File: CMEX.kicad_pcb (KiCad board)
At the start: 2 copper layers, 4 parts, among them U1 DAC63004RTET, U2 TPS62151, U3 ADS8584S

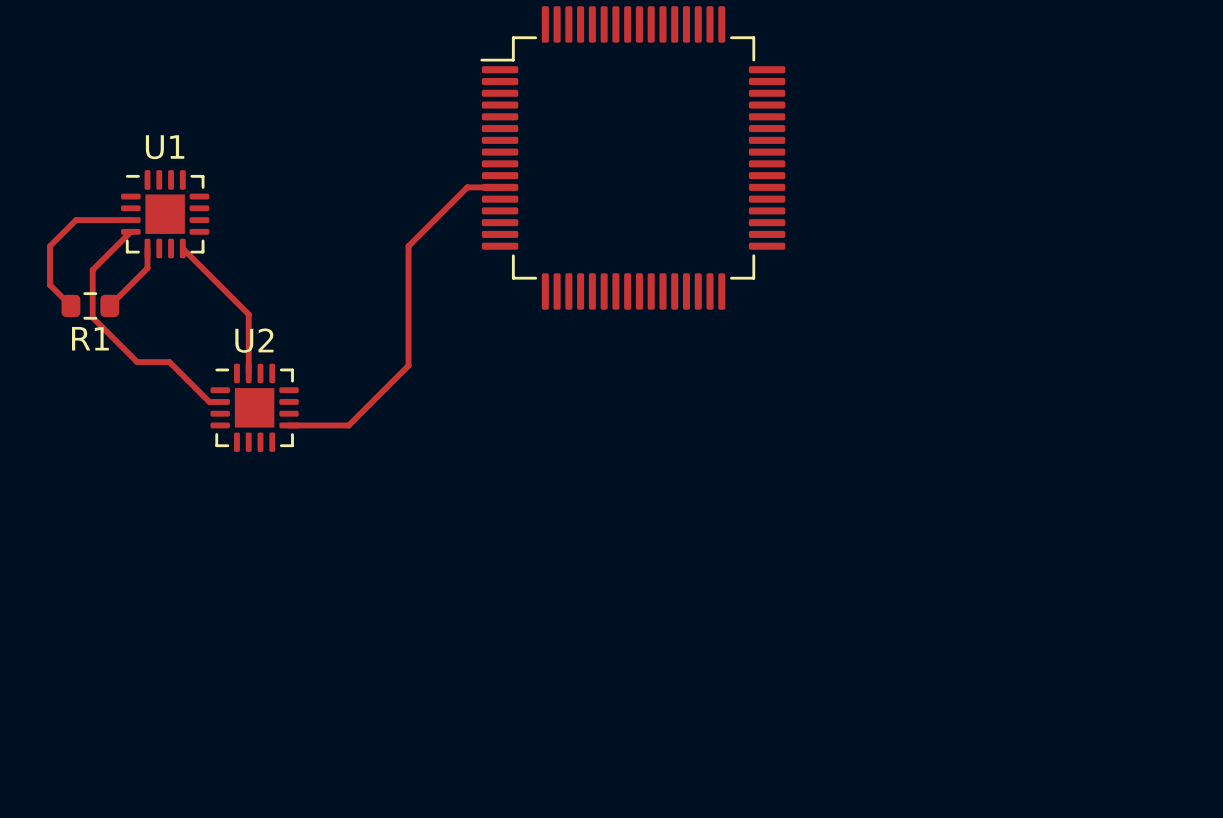
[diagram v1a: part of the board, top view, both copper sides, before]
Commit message: Added connector to all sheets.
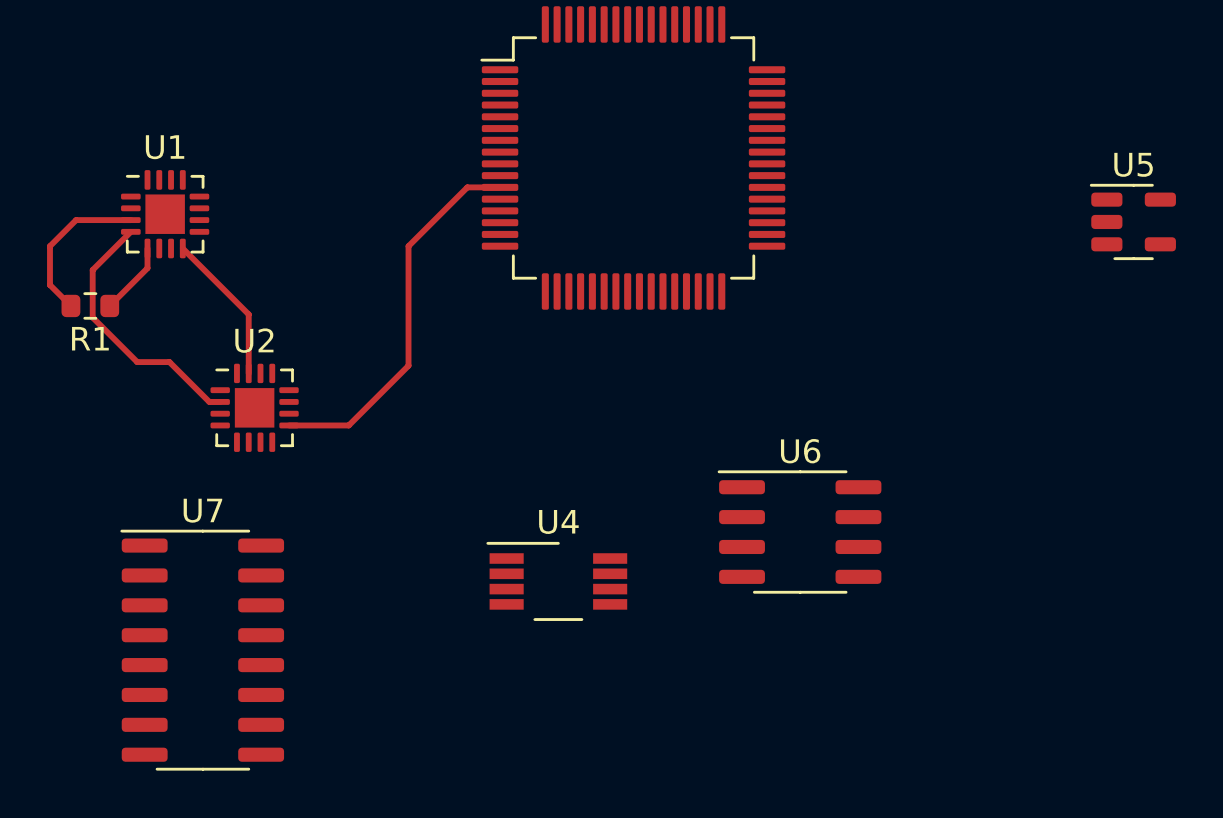
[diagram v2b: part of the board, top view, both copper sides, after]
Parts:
- added U4: TLV8802, Package_SO:VSSOP-8_3.0x3.0mm_P0.65mm, F.Cu at (67.3, 44.7)
- added U5: TLV8801, Package_TO_SOT_SMD:SOT-23-5, F.Cu at (91.8, 29.4)
- added U6: LMC7660, Package_SO:SOIC-8_3.9x4.9mm_P1.27mm, F.Cu at (77.6, 42.6)
- added U7: SN65MLVD047AD, Package_SO:SOIC-16_3.9x9.9mm_P1.27mm, F.Cu at (52.2, 47.6)

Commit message: Layout erster Entwurf fertig.
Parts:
- removed U4: TLV8802, Package_SO:VSSOP-8_3.0x3.0mm_P0.65mm
- added C1: C0402_100nF_50V, Capacitor_SMD:C_0402_1005Metric, F.Cu at (183.4, 132.6)
- added C10: C0402_22uF_6.3V, Capacitor_SMD:C_0402_1005Metric, F.Cu at (173.2, 139.8)
- added C11: C0402_1uF_6.3V, Capacitor_SMD:C_0402_1005Metric, F.Cu at (192.6, 139.1)
- added C12: C0402_100nF_50V, Capacitor_SMD:C_0402_1005Metric, F.Cu at (192.6, 138.1)
- added C15: C0402_330p_25V, Capacitor_SMD:C_0402_1005Metric, F.Cu at (182.0, 141.9)
- added C17: C0402_10uF_6.3V, Capacitor_SMD:C_0402_1005Metric, F.Cu at (182.0, 139.8)
- added C19: C0402_22uF_6.3V, Capacitor_SMD:C_0402_1005Metric, F.Cu at (183.3, 139.9)
- added C2: C0402_4.7uF_6.3V, Capacitor_SMD:C_0402_1005Metric, F.Cu at (184.7, 132.6)
- added C21: C0402_1uF_6.3V, Capacitor_SMD:C_0402_1005Metric, F.Cu at (196.0, 138.7)
- added C22: C0402_1uF_6.3V, Capacitor_SMD:C_0402_1005Metric, F.Cu at (197.8, 153.0)
- added C23: C0402_100nF_50V, Capacitor_SMD:C_0402_1005Metric, F.Cu at (197.8, 139.4)
- added C24: C0402_100nF_50V, Capacitor_SMD:C_0402_1005Metric, F.Cu at (197.3, 154.7)
- added C25: C0402_1uF_6.3V, Capacitor_SMD:C_0402_1005Metric, F.Cu at (189.2, 155.1)
- added C26: C0402_1uF_6.3V, Capacitor_SMD:C_0402_1005Metric, F.Cu at (183.8, 147.0)
- added C27: C0402_100nF_50V, Capacitor_SMD:C_0402_1005Metric, F.Cu at (190.3, 155.1)
- added C28: C0402_100nF_50V, Capacitor_SMD:C_0402_1005Metric, F.Cu at (183.8, 145.8)
- added C3: C0402_100nF_50V, Capacitor_SMD:C_0402_1005Metric, F.Cu at (183.3, 135.3)
- added C31: C0402_10uF_6.3V, Capacitor_SMD:C_0402_1005Metric, F.Cu at (194.2, 155.1)
- added C32: C0402_10uF_6.3V, Capacitor_SMD:C_0402_1005Metric, F.Cu at (193.0, 155.1)
- added C33: C0402_1uF_6.3V, Capacitor_SMD:C_0402_1005Metric, F.Cu at (191.6, 155.1)
- added C34: C0402_1uF_6.3V, Capacitor_SMD:C_0402_1005Metric, F.Cu at (188.0, 155.1)
- added C35: C0402_10nF_16V, Capacitor_SMD:C_0402_1005Metric, F.Cu at (214.9, 144.3)
- added C37: C0402_1uF_6.3V, Capacitor_SMD:C_0402_1005Metric, F.Cu at (216.0, 144.3)
- added C39: C0402_100nF_50V, Capacitor_SMD:C_0402_1005Metric, F.Cu at (217.2, 144.3)
- added C4: C0402_4.7uF_6.3V, Capacitor_SMD:C_0402_1005Metric, F.Cu at (184.6, 135.3)
- added C41: C0402_10nF_16V, Capacitor_SMD:C_0402_1005Metric, F.Cu at (211.6, 151.3)
- added C42: C0402_10nF_16V, Capacitor_SMD:C_0402_1005Metric, F.Cu at (206.8, 153.0)
- added C43: C0402_1uF_6.3V, Capacitor_SMD:C_0402_1005Metric, F.Cu at (210.6, 151.3)
- added C44: C0402_1uF_6.3V, Capacitor_SMD:C_0402_1005Metric, F.Cu at (206.8, 152.0)
- added C45: C0402_100nF_50V, Capacitor_SMD:C_0402_1005Metric, F.Cu at (212.7, 151.3)
- added C46: C0402_100nF_50V, Capacitor_SMD:C_0402_1005Metric, F.Cu at (206.8, 150.9)
- added C47: C0402_10nF_16V, Capacitor_SMD:C_0402_1005Metric, F.Cu at (217.1, 146.5)
- added C49: C0402_1uF_6.3V, Capacitor_SMD:C_0402_1005Metric, F.Cu at (215.0, 146.5)
- added C5: C0402_560p_10V, Capacitor_SMD:C_0402_1005Metric, F.Cu at (190.4, 136.1)
- added C51: C0402_100nF_50V, Capacitor_SMD:C_0402_1005Metric, F.Cu at (216.1, 146.5)
- added C53: C0402_10nF_16V, Capacitor_SMD:C_0402_1005Metric, F.Cu at (217.1, 148.6)
- added C54: C0402_1uF_6.3V, Capacitor_SMD:C_0402_1005Metric, F.Cu at (214.9, 148.6)
- added C55: C0402_10nF_16V, Capacitor_SMD:C_0402_1005Metric, F.Cu at (206.9, 139.2)
- added C56: C0402_100nF_50V, Capacitor_SMD:C_0402_1005Metric, F.Cu at (216.0, 148.6)
- added C57: C0402_100nF_50V, Capacitor_SMD:C_0402_1005Metric, F.Cu at (208.4, 151.2)
- added C58: C0402_1uF_6.3V, Capacitor_SMD:C_0402_1005Metric, F.Cu at (206.9, 140.3)
- added C59: C0402_100nF_50V, Capacitor_SMD:C_0402_1005Metric, F.Cu at (209.4, 151.2)
- added C6: C0402_330p_25V, Capacitor_SMD:C_0402_1005Metric, F.Cu at (172.7, 143.8)
- added C60: C0402_100nF_50V, Capacitor_SMD:C_0402_1005Metric, F.Cu at (206.9, 141.4)
- added C61: C0402_1uF_6.3V, Capacitor_SMD:C_0402_1005Metric, F.Cu at (169.0, 154.2)
- added C62: C0402_100nF_50V, Capacitor_SMD:C_0402_1005Metric, F.Cu at (169.0, 153.2)
- added C63: C0402_1uF_6.3V, Capacitor_SMD:C_0402_1005Metric, F.Cu at (177.7, 156.8)
- added C64: C0402_100nF_50V, Capacitor_SMD:C_0402_1005Metric, F.Cu at (176.2, 158.3)
- added C66: C0402_100nF_50V, Capacitor_SMD:C_0402_1005Metric, F.Cu at (166.8, 148.1)
- added C67: C0402_100nF_50V, Capacitor_SMD:C_0402_1005Metric, F.Cu at (175.5, 148.4)
- added C7: C0402_10uF_6.3V, Capacitor_SMD:C_0402_1005Metric, F.Cu at (173.2, 141.8)
- added C8: C0402_100nF_50V, Capacitor_SMD:C_0402_1005Metric, F.Cu at (190.9, 131.2)
- added C9: C0402_4.7uF_6.3V, Capacitor_SMD:C_0402_1005Metric, F.Cu at (190.9, 132.3)
- added J1: Conn_01x30, Connector_PinHeader_1.27mm:PinHeader_1x30_P1.27mm_Vertical, F.Cu at (192.3, 128.1)
- added L1: 2.2uH, Inductor_SMD:L_Coilcraft_XAL60xx_6.36x6.56mm, F.Cu at (170.3, 134.5)
- added L2: 2.2uH, Inductor_SMD:L_Coilcraft_XAL60xx_6.36x6.56mm, F.Cu at (178.6, 134.7)
- added R13: R0402_100, Resistor_SMD:R_0402_1005Metric, F.Cu at (203.4, 144.0)
- added R14: R0402_33k, Resistor_SMD:R_0402_1005Metric, F.Cu at (165.6, 149.1)
- added R15: R0402_33k, Resistor_SMD:R_0402_1005Metric, F.Cu at (176.8, 149.5)
- added R16: R0402_10k, Resistor_SMD:R_0402_1005Metric, F.Cu at (166.8, 150.2)
- added R17: R0402_10k, Resistor_SMD:R_0402_1005Metric, F.Cu at (175.4, 150.7)
- added R18: R0402_56k, Resistor_SMD:R_0402_1005Metric, F.Cu at (171.8, 146.5)
- added R19: R0402_33k, Resistor_SMD:R_0402_1005Metric, F.Cu at (173.9, 146.5)
- added R2: R0402_150k, Resistor_SMD:R_0402_1005Metric, F.Cu at (166.0, 142.2)
- added R3: R0402_100k, Resistor_SMD:R_0402_1005Metric, F.Cu at (167.4, 140.0)
- added R4: R0402_105k, Resistor_SMD:R_0402_1005Metric, F.Cu at (186.3, 131.4)
- added R5: R0402_6.19k, Resistor_SMD:R_0402_1005Metric, F.Cu at (190.4, 133.9)
- added R6: R0402_4.99k, Resistor_SMD:R_0402_1005Metric, F.Cu at (191.8, 135.0)
- added R7: R0402_120k, Resistor_SMD:R_0402_1005Metric, F.Cu at (174.9, 139.8)
- added R8: R0402_22k, Resistor_SMD:R_0402_1005Metric, F.Cu at (174.9, 141.8)
- added R9: R0402_100k, Resistor_SMD:R_0402_1005Metric, F.Cu at (176.2, 139.8)
- added U10: MCP4728-E_UN, Package_SO:MSOP-10_3x3mm_P0.5mm, F.Cu at (173.4, 155.7)
- added U8: ~, Package_TO_SOT_SMD:SOT-23-5, F.Cu at (203.3, 141.5)
- added U9: TLC2272, Package_SO:SO-8_3.9x4.9mm_P1.27mm, F.Cu at (171.2, 149.8)
- R1: value R0603_470 -> R0402_215k; footprint Resistor_SMD:R_0603_1608Metric -> Resistor_SMD:R_0402_1005Metric
- U1: value DAC63004RTET -> TPS74801; footprint Package_DFN_QFN:WQFN-16-1EP_3x3mm_P0.5mm_EP1.68x1.68mm -> Package_SON:VSON-10-1EP_3x3mm_P0.5mm_EP1.65x2.4mm
- U3: value ADS8584S -> TPS62151; footprint Package_QFP:LQFP-64_10x10mm_P0.5mm -> Package_DFN_QFN:VQFN-16-1EP_3x3mm_P0.5mm_EP1.68x1.68mm
- U5: value TLV8801 -> ADS8584S; footprint Package_TO_SOT_SMD:SOT-23-5 -> Package_QFP:LQFP-64_10x10mm_P0.5mm
- U6: value LMC7660 -> ~; footprint Package_SO:SOIC-8_3.9x4.9mm_P1.27mm -> Package_SO:SSOP-16_4.4x5.2mm_P0.65mm
- U7: value SN65MLVD047AD -> ~; footprint Package_SO:SOIC-16_3.9x9.9mm_P1.27mm -> Package_DFN_QFN:HVQFN-40-1EP_6x6mm_P0.5mm_EP4.1x4.1mm
- moved U7 185.9 mm to (209.7, 146.6)
- moved U1 172.6 mm to (187.5, 134.2)
- moved U6 165.6 mm to (213.1, 138.0), turned to 90 degrees
- moved R1 159.7 mm to (166.0, 140.0), turned to 90 degrees
- moved U3 157.4 mm to (179.1, 140.8)
- moved U2 155.6 mm to (170.4, 141.1)
- moved U5 154.4 mm to (192.3, 146.6), turned to -90 degrees
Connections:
- R1 pad 1: Net-(U1-GPIO/SDO) -> Net-(U2-FB)
- R1 pad 2: Net-(U1-OUT2) -> /Power_suppy/2V
- U1 pad 1: unconnected-(U1-FB3-Pad1) -> /Power_suppy/2V
- U1 pad 10: unconnected-(U1-OUT1-Pad10) -> 1V8a
- U1 pad 11: unconnected-(U1-OUT0-Pad11) -> GND
- U1 pad 2: unconnected-(U1-OUT3-Pad2) -> /Power_suppy/2V
- U1 pad 3: Net-(U1-OUT2) -> Net-(U1-PG)
- U1 pad 4: Net-(U1-FB2) -> Net-(U1-BIAS)
- U1 pad 5: Net-(U1-GPIO/SDO) -> /Power_suppy/2V
- U1 pad 6: unconnected-(U1-SCL/nSYNC-Pad6) -> GND
- U1 pad 7: unconnected-(U1-A0/SDI-Pad7) -> Net-(U1-SS)
- U1 pad 8: Net-(U1-SDA/SCLK) -> Net-(U1-FB)
- U1 pad 9: unconnected-(U1-FB1-Pad9) -> 1V8a
- U2 pad 1: unconnected-(U2-SW-Pad1) -> Net-(L1-Pad1)
- U2 pad 10: unconnected-(U2-AVIN-Pad10) -> 5V
- U2 pad 11: unconnected-(U2-PVIN-Pad11) -> 5V
- U2 pad 12: unconnected-(U2-PVIN-Pad12) -> 5V
- U2 pad 13: unconnected-(U2-EN-Pad13) -> /Power_suppy/ENABLE_PWR
- U2 pad 14: unconnected-(U2-VOS-Pad14) -> /Power_suppy/2V
- U2 pad 15: Net-(U1-SDA/SCLK) -> GND
- U2 pad 16: unconnected-(U2-PGND-Pad16) -> GND
- U2 pad 17: unconnected-(U2-THERM-Pad17) -> GND
- U2 pad 2: Net-(U1-FB2) -> Net-(L1-Pad1)
- U2 pad 3: unconnected-(U2-SW-Pad3) -> Net-(L1-Pad1)
- U2 pad 4: unconnected-(U2-PG-Pad4) -> Net-(U2-PG)
- U2 pad 5: unconnected-(U2-FB-Pad5) -> Net-(U2-FB)
- U2 pad 6: unconnected-(U2-AGND-Pad6) -> GND
- U2 pad 7: unconnected-(U2-FSW-Pad7) -> /Power_suppy/2V
- U2 pad 8: unconnected-(U2-DEF-Pad8) -> GND
- U3 pad 1: unconnected-(U3-AVDD-Pad1) -> Net-(L2-Pad1)
- U3 pad 10: unconnected-(U3-CONVSTB-Pad10) -> 5V
- U3 pad 11: Net-(U2-SS/TR) -> 5V
- U3 pad 12: unconnected-(U3-nRD/SCLK-Pad12) -> 5V
- U3 pad 13: unconnected-(U3-nCS-Pad13) -> /Power_suppy/ENABLE_PWR
- U3 pad 14: unconnected-(U3-BUSY-Pad14) -> GND
- U3 pad 15: unconnected-(U3-FRSTDATA-Pad15) -> -5V
- U3 pad 16: unconnected-(U3-DB0-Pad16) -> -5V
- U3 pad 17: unconnected-(U3-DB1-Pad17) -> GND
- U3 pad 2: unconnected-(U3-AGND-Pad2) -> Net-(L2-Pad1)
- U3 pad 3: unconnected-(U3-OS0-Pad3) -> Net-(L2-Pad1)
- U3 pad 4: unconnected-(U3-OS1-Pad4) -> Net-(U3-PG)
- U3 pad 5: unconnected-(U3-OS2-Pad5) -> Net-(U3-FB)
- U3 pad 6: unconnected-(U3-nPAR/SER/BYTE_SEL-Pad6) -> -5V
- U3 pad 7: unconnected-(U3-nSTBY-Pad7) -> GND
- U3 pad 8: unconnected-(U3-RANGE-Pad8) -> -5V
- U3 pad 9: unconnected-(U3-CONVSTA-Pad9) -> Net-(U3-SS/TR)
- U5 pad 1: unconnected-(U5-Pad1) -> 5V
- U5 pad 2: unconnected-(U5-V--Pad2) -> GND
- U5 pad 3: unconnected-(U5-+-Pad3) -> /ADC/OS0
- U5 pad 4: unconnected-(U5---Pad4) -> /ADC/OS1
- U5 pad 5: unconnected-(U5-V+-Pad5) -> /ADC/OS2
- U6 pad 1: unconnected-(U6-N/C-Pad1) -> /AWAGS/iSEL
- U6 pad 2: unconnected-(U6-Cap+-Pad2) -> /AWAGS/SEL_P
- U6 pad 3: unconnected-(U6-GND-Pad3) -> /AWAGS/SEL_M
- U6 pad 4: unconnected-(U6-Cap--Pad4) -> 3V3
- U6 pad 5: unconnected-(U6-Vout-Pad5) -> /AWAGS/SCLK_P
- U6 pad 6: unconnected-(U6-LV-Pad6) -> /AWAGS/SCLK_M
- U6 pad 7: unconnected-(U6-Osc-Pad7) -> /AWAGS/iCLK
- U6 pad 8: unconnected-(U6-V+-Pad8) -> GND
- U7 pad 1: unconnected-(U7-EN-Pad1) -> /AWAGS/DO_P
- U7 pad 10: unconnected-(U7-4Y-Pad10) -> /ADC/OUT0_P
- U7 pad 11: unconnected-(U7-3Y-Pad11) -> GND
- U7 pad 12: unconnected-(U7-3Z-Pad12) -> 1V8a
- U7 pad 14: unconnected-(U7-2Y-Pad14) -> Net-(U7-DAC_SET)
- U7 pad 15: unconnected-(U7-1Y-Pad15) -> Net-(U7-AUTO_SET)
- U7 pad 16: unconnected-(U7-1Z-Pad16) -> 1V8a
- U7 pad 2: unconnected-(U7-1A-Pad2) -> /AWAGS/DO_M
- U7 pad 3: unconnected-(U7-2A-Pad3) -> /ADC/OUT3_M
- U7 pad 4: unconnected-(U7-VCC-Pad4) -> /ADC/OUT3_P
- U7 pad 5: unconnected-(U7-GND-Pad5) -> /ADC/OUT2_M
- U7 pad 6: unconnected-(U7-3A-Pad6) -> /ADC/OUT2_P
- U7 pad 7: unconnected-(U7-4A-Pad7) -> /ADC/OUT1_M
- U7 pad 8: unconnected-(U7-nEN-Pad8) -> /ADC/OUT1_P
- U7 pad 9: unconnected-(U7-4Z-Pad9) -> /ADC/OUT0_M
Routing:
- net /DAC/VBIAS2: track 0.00 -> 79.2 mm, vias 0 -> 2
- net /DAC/~{LDAC_DAC_REF}: track 0.00 -> 73.5 mm, vias 0 -> 2
- net /DAC/VBIAS1: track 0.00 -> 73.0 mm, vias 0 -> 2
- net /DAC/SDA_DAC_REF: track 0.00 -> 72.9 mm, vias 0 -> 2
- net /DAC/SCL_DAC_REF: track 0.00 -> 72.4 mm, vias 0 -> 2
- net /Power_suppy/ENABLE_PWR: track 0.00 -> 67.6 mm, vias 0 -> 3
- net /Power_suppy/2V: track 0.00 -> 50.6 mm, vias 0 -> 5
- net 1V8a: track 0.00 -> 44.6 mm, vias 0 -> 8
- net -5V: track 0.00 -> 43.5 mm, vias 0 -> 3
- net /ADC/DATA: track 0.00 -> 36.7 mm, vias 0 -> 4
- net 5V: track 0.00 -> 34.7 mm, vias 0 -> 6
- net 3V3: track 0.00 -> 33.2 mm, vias 0 -> 9
- net /AWAGS/AIN0: track 0.00 -> 32.5 mm, vias 0 -> 3
- net /ADC/FIRST: track 0.00 -> 31.9 mm, vias 0 -> 2
- net GND: track 0.00 -> 31.3 mm, vias 0 -> 3
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- added copper zone on In5.Cu, net 1V8a
- added copper zone on In1.Cu, net 3V3
- added copper zone on In6.Cu, net 5V
- added copper zone on B.Cu, net GND
- added copper zone on F.Cu, net GND
- added copper zone on In2.Cu, net GND
- added copper zone on In3.Cu, net GND
- added copper zone on In4.Cu, net GND
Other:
- board outline added: 95.3 x 90.2 mm
- copper layers 2 -> 8

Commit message: Kleine Änderung.
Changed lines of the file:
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@@
     )
   )
+  (gr_rect (start 165.4 140.725) (end 190.775 165.25)
+    (stroke (width 0.2) (type default)) (fill none) (layer "F.Cu"))
   (gr_rect (start 94.375 102.325) (end 120.55 111.325)
     (stroke (width 0.15) (type default)) (fill none) (layer "B.Paste"))
